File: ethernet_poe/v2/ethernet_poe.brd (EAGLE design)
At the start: 45.5 x 50.5 mm, 94 parts, among them J3 ARJM11C7-104-AB-EW2, Q1 BSR16, U1 AZ1117EH-3.3TRG1, U2 IFX91041, U3 W5500, U4 TPS26600PWPR, X1 25MHz

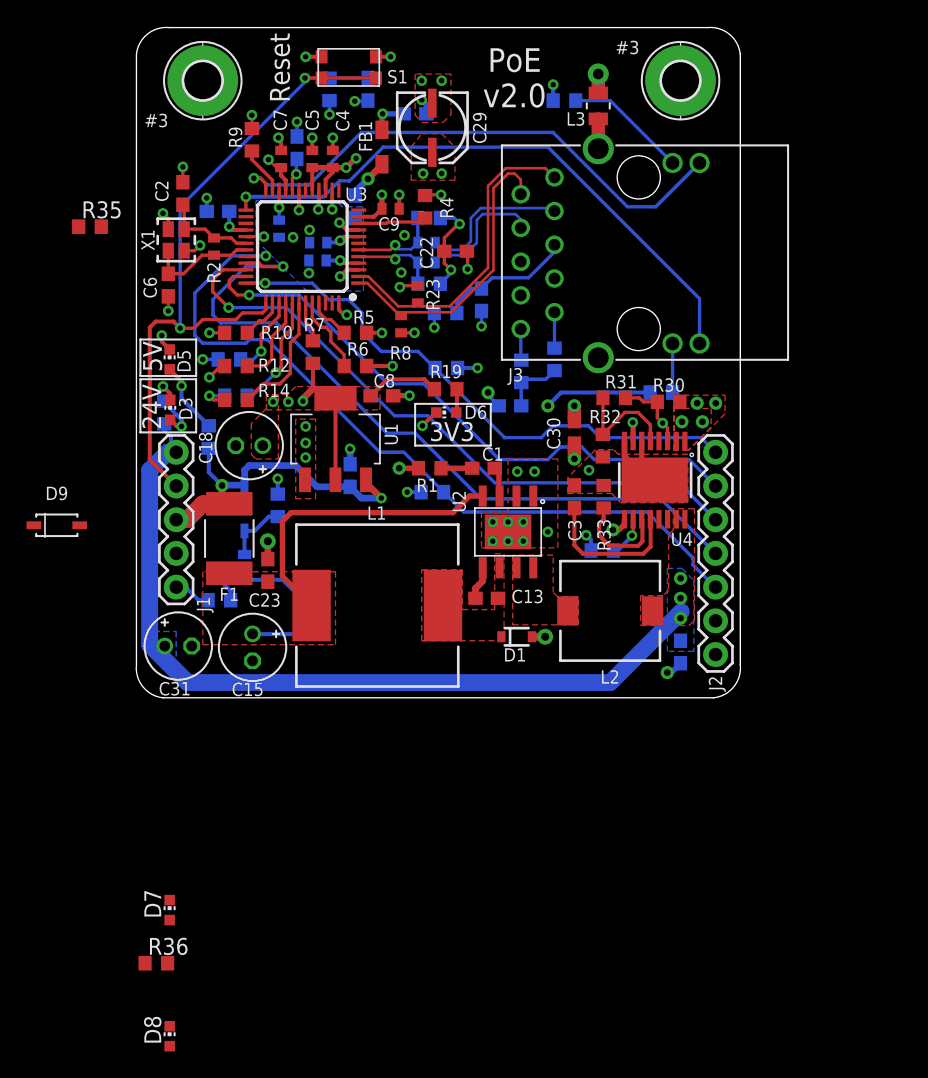
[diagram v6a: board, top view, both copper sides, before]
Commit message: post design review routing updates
replaced 5V DC/DC converter catch diode
routed Wiznet LEDs
added thermal pads to efuse and DC/DC converters
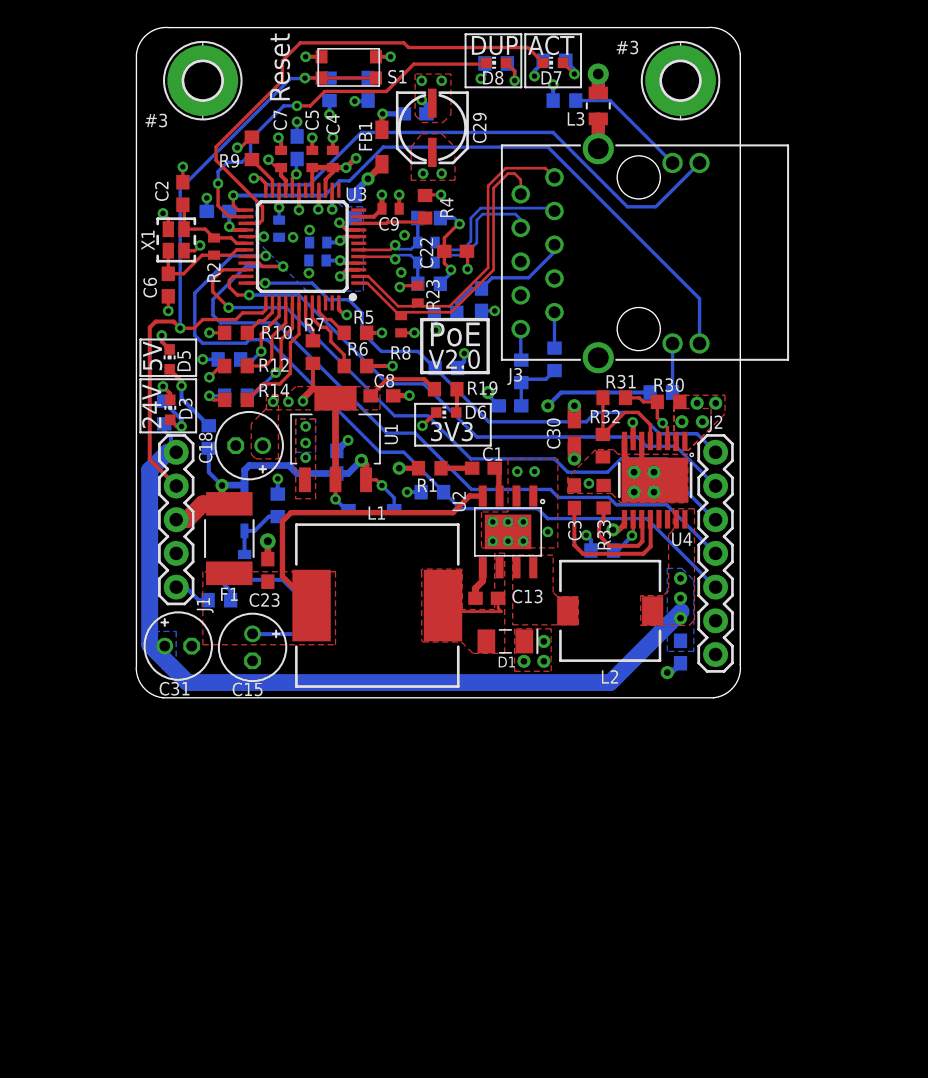
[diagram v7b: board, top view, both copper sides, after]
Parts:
- D1: value (none) -> NTS260ESFT3G; device RoboJackets-Diodes:SOD-323 -> ethernet_poe:DIO_SS26FL
- moved D8 77.4 mm to (27.1, 47.9), turned to 90 degrees
- moved R36 72.5 mm to (27.1, 47.8), flipped to the bottom, turned to 180 degrees
- moved D7 70.1 mm to (31.4, 47.9), turned to 90 degrees
- moved R35 37.2 mm to (31.5, 48.0), flipped to the bottom, turned to 180 degrees
- moved D9 23.7 mm to (17.7, 14.3), flipped to the bottom
- moved C16 1.41 mm to (15.1, 17.8)
- moved D1 0.92 mm to (27.8, 4.25)
- moved R9 0.65 mm to (8.70, 41.4)
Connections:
- net 5V_RAW: now also D1.1; no longer D1.C
- net AGND: now also H1.B2,8, H2.B2,8
- net GND: now also D1.2; no longer D1.A, H1.B2,8, H2.B2,8
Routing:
- net AGND: track 2.25 -> 54.3 mm
- net ACTLED: track 0.00 -> 37.7 mm
- net DUPLED: track 0.00 -> 29.3 mm, vias 0 -> 2
- net 5V_RAW: track 0.00 -> 5.69 mm
- net +3V3_D: track 36.3 -> 41.5 mm, vias 12 -> 15
- net 3V3_LED2: track 0.00 -> 3.15 mm, vias 0 -> 1
- net 3V3_LED1: track 0.00 -> 2.47 mm, vias 0 -> 1
- net LINKLED: track 44.8 -> 46.6 mm
- net MISO: track 48.7 -> 50.1 mm
- net +5V: track 25.3 -> 26.6 mm, vias 2 -> 3
- net RTN: track 12.8 -> 11.8 mm, vias 2 -> 6
- net MOSI: track 45.5 -> 44.7 mm
- net GND: track 57.9 -> 57.2 mm, vias 62 -> 64
- net N$1: track 3.59 -> 2.94 mm
- net !RST: track 55.8 -> 56.5 mm
- added copper zone on layer 16, net RTN
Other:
- board text added: "ACT"
- board text added: "DUP"
- board text added: "PoE"
- board text added: "V2.0"
- board text removed: "PoE v2.0"

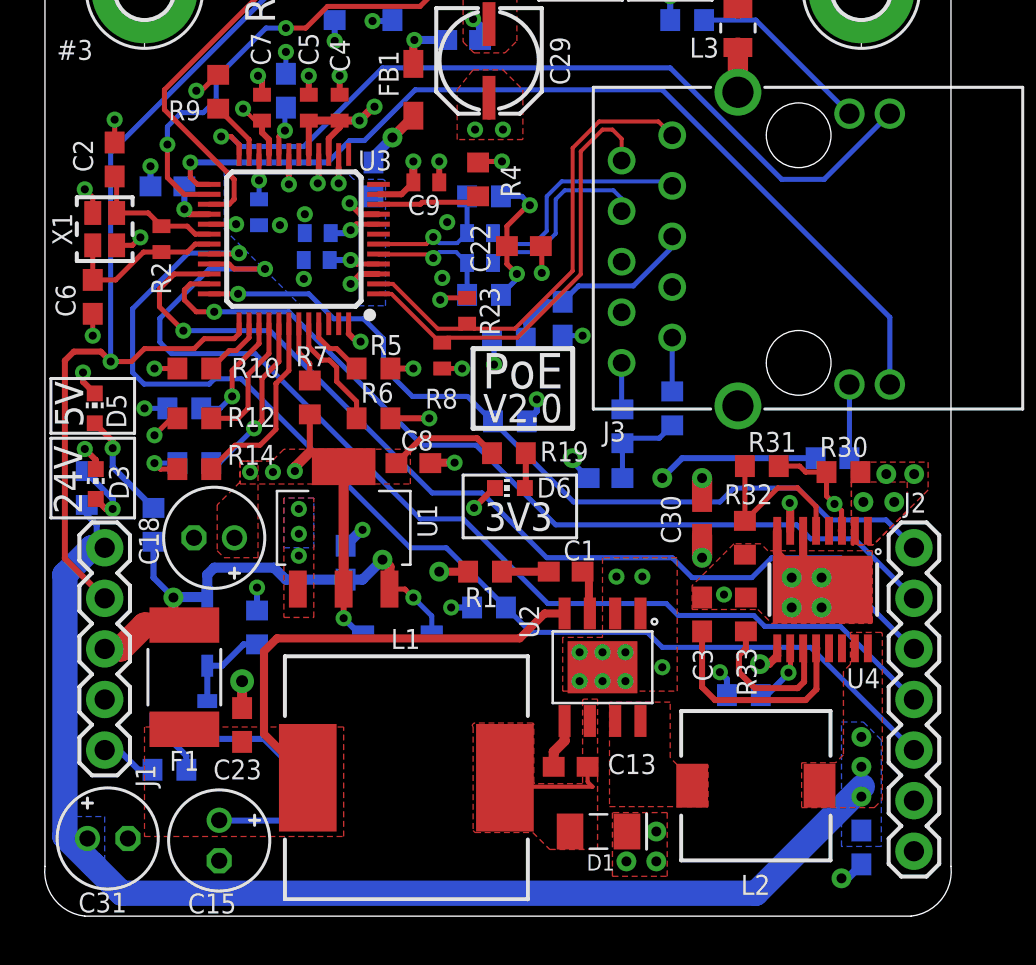
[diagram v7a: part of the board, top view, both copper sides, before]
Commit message: final changes, created manufacturing output
- Modified layer stackup to match AllPCB standard 4-layer
- Modified MDI trace widths and spacing for 100ohm differential impedance control
- Generated manufacturing CAM files
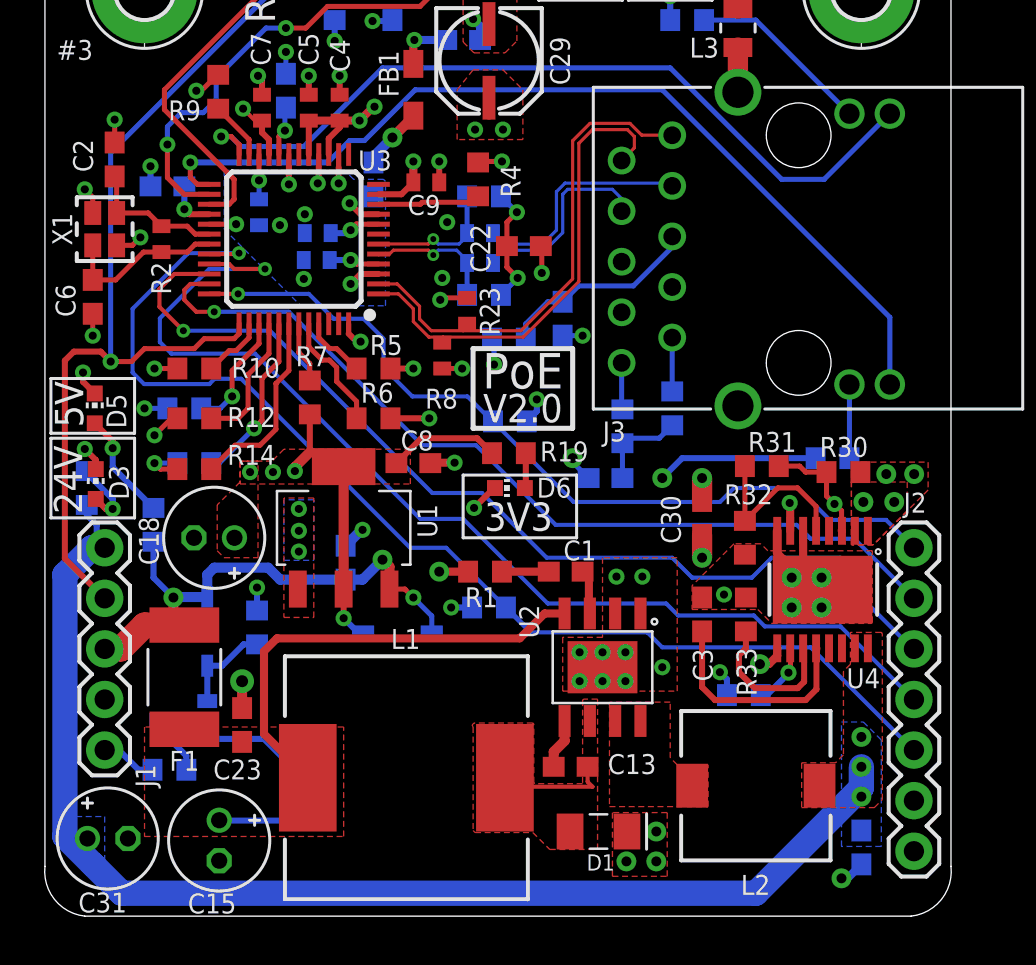
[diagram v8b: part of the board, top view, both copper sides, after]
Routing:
- net TX_N: track 22.6 -> 24.4 mm
- net RX_FILTER: track 7.24 -> 6.06 mm
- net TX_P: track 24.1 -> 25.2 mm
- net +24V_FUSE: track 62.4 -> 63.4 mm
